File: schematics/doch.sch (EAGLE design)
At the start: 6 parts

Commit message: Продолжение работы над платами
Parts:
- added LP5907MFX-3.3: (no value), CanCubeSat:LP5907MFX-3.3
- added U$1: SD, CanCubeSat:SD

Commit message: 3я часть Дочернего балета
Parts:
- removed STM32F103C8T: STM32F103C8T, CanCubeSat:STM32F103C8T
- removed TOMOM: (no value), pinhead:PINHD-1X2
- added BUZZER: BUZZER, CanCubeSat:BUZZER
- added C1: 1nF, rcl:C-EUC0603
- added C15, C5, C6, C7, C8: 100nF, rcl:C-EUC0603
- added C16: 10µ, rcl:C-USC1206
- added C2: 10nF, rcl:C-EUC0603
- added IC2: STM32F103C8T, CanCubeSat:STM32F103C8T
- added JP1: (no value), pinhead:PINHD-1X5
- added PB5, PWR: (no value), led:LEDCHIPLED_0603
- added R1: 100R, rcl:R-US_R0603
- added R2: 10k, rcl:R-US_R0603
- added R27, R64, R79: 10k, resistor:R-US_R0603
- added R3: (no value), rcl:R-US_R0603
- added R81, R82: 2k, resistor:R-US_R0603
- added SD-PORT: SD, CanCubeSat:SD
- added TCXO: OC2E08000XCCDRX, CanCubeSat:OC2E08000XCCDRX
- added TOMA: (no value), pinhead:PINHD-1X2/90
- U$1: value SD -> SI2302CDS; device CanCubeSat:SD -> CanCubeSat:SI2302CDS
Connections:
- new net 3V3: C15.1, C16.1, C2.2, C5.1, C6.1, C7.1, C8.1, IC2.VBAT, IC2.VDD, IC2.VDDA, PB5.A, PWR.A, R27.1, R64.1, R79.1, TCXO.EN/DIS, TCXO.VCC
- new net 3V7: SUPPLY.1
- new net GND: C15.2, C16.2, C2.1, C5.2, C6.2, C7.2, C8.2, IC2.BOOT0, IC2.PB2, IC2.VSSA, R3.2, R82.1, SUPPLY.2, TCXO.GND, TOMA.2
- new net N$1: BUZZER.-, U$1.D
- new net N$10: R3.1
- new net N$159: PWR.C, R82.2
- new net N$161: IC2.PB5, R81.1
- new net N$17: PB5.C, R81.2
- new net N$2: R1.2, U$1.G
- new net N$3: R1.1, R2.2, U$1.S
- new net N$4: C1.2, TCXO.OUTPUT
- new net N$5: C1.1, IC2.OSC_IN
- new net N$6: R2.1
- new net N$7: BUZZER.+
- new net NRST: IC2.NRST, R79.2
- new net PE12: TOMA.1
- new net SWC: IC2.PA14, R27.2
- new net SWD: IC2.PA13, R64.2
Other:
- note added: "Микроконтроллер"
- moved on the sheet: BME280, GOOUUUATGM336H, LP5907MFX-3.3, LSM6DS3, SUPPLY

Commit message: Актуальная версия плат (и библиотеки)
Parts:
- removed SD-PORT: SD, CanCubeSat:SD
- added C10, C9: 1μF, rcl:C-EUC0603
- added C11, C12, C3, C4: 100nF, rcl:C-EUC0603
- added R4: 10K, rcl:R-US_R0603
- added R5: 100R, rcl:R-US_R0603
- added SD: SD-SPI, CanCubeSat:SD-SPI
- R3: value (none) -> 10K
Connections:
- removed net N$10: R3.1
- removed net N$3: R1.1, R2.2, U$1.S
- removed net N$6: R2.1
- removed net N$7: BUZZER.+
- removed net PE12: TOMA.1
- new net N$12: IC2.PC15
- new net N$8: R3.1, R5.1, TOMA.1
- new net N$9: IC2.PB0, R3.2
- new net PB1-BUZZER: IC2.PB1, R1.1, R2.2, U$1.S
- new net SPI1_CS_BME280: BME280.CSB, IC2.PC13
- new net SPI1_CS_LSM6DS3: IC2.PC14, LSM6DS3.CS
- new net SPI1_MISO: BME280.SDO, IC2.PA6, LSM6DS3.SA0
- new net SPI1_MOSI: BME280.SDI, IC2.PA7, LSM6DS3.SDA
- new net SPI1_SCK: BME280.SCK, IC2.PA5, LSM6DS3.SCL
- new net SPI2_CS_SD: IC2.PB12, SD.CS
- new net SPI2_MISO: IC2.PB14, R4.1, SD.DO
- new net SPI2_MOSI: IC2.PB15, SD.DI
- new net SPI2_SCK: IC2.PB13, SD.SCLK
- new net USART3_RX: GOOUUUATGM336H.TX, IC2.PB11
- new net USART3_TX: GOOUUUATGM336H.RX, IC2.PB10
- new net WKUP: IC2.PA0-WKUP, JP1.1
- net 3V3: now also BME280.VDD, BME280.VIO, BUZZER.+, C10.2, C11.2, C12.1, C3.2, C4.1, GOOUUUATGM336H.VCC, JP1.4, LP5907MFX-3.3.OUT, LSM6DS3.INT2, LSM6DS3.VDD, R5.2, SD.VDD
- net 3V7: now also C9.2, LP5907MFX-3.3.EN, LP5907MFX-3.3.IN
- net GND: now also BME280.GND, C10.1, C11.1, C12.2, C3.1, C4.2, C9.1, GOOUUUATGM336H.GND, LP5907MFX-3.3.GND, LSM6DS3.GND, LSM6DS3.SCX, LSM6DS3.SDX, R2.1, R4.2, SD.VSS; no longer R3.2
- net NRST: now also JP1.5
- net SWC: now also JP1.2
- net SWD: now also JP1.3
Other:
- moved on the sheet: BUZZER, C1, C15, C16, C2, C5, C6, C7, C8, IC2, JP1, LP5907MFX-3.3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

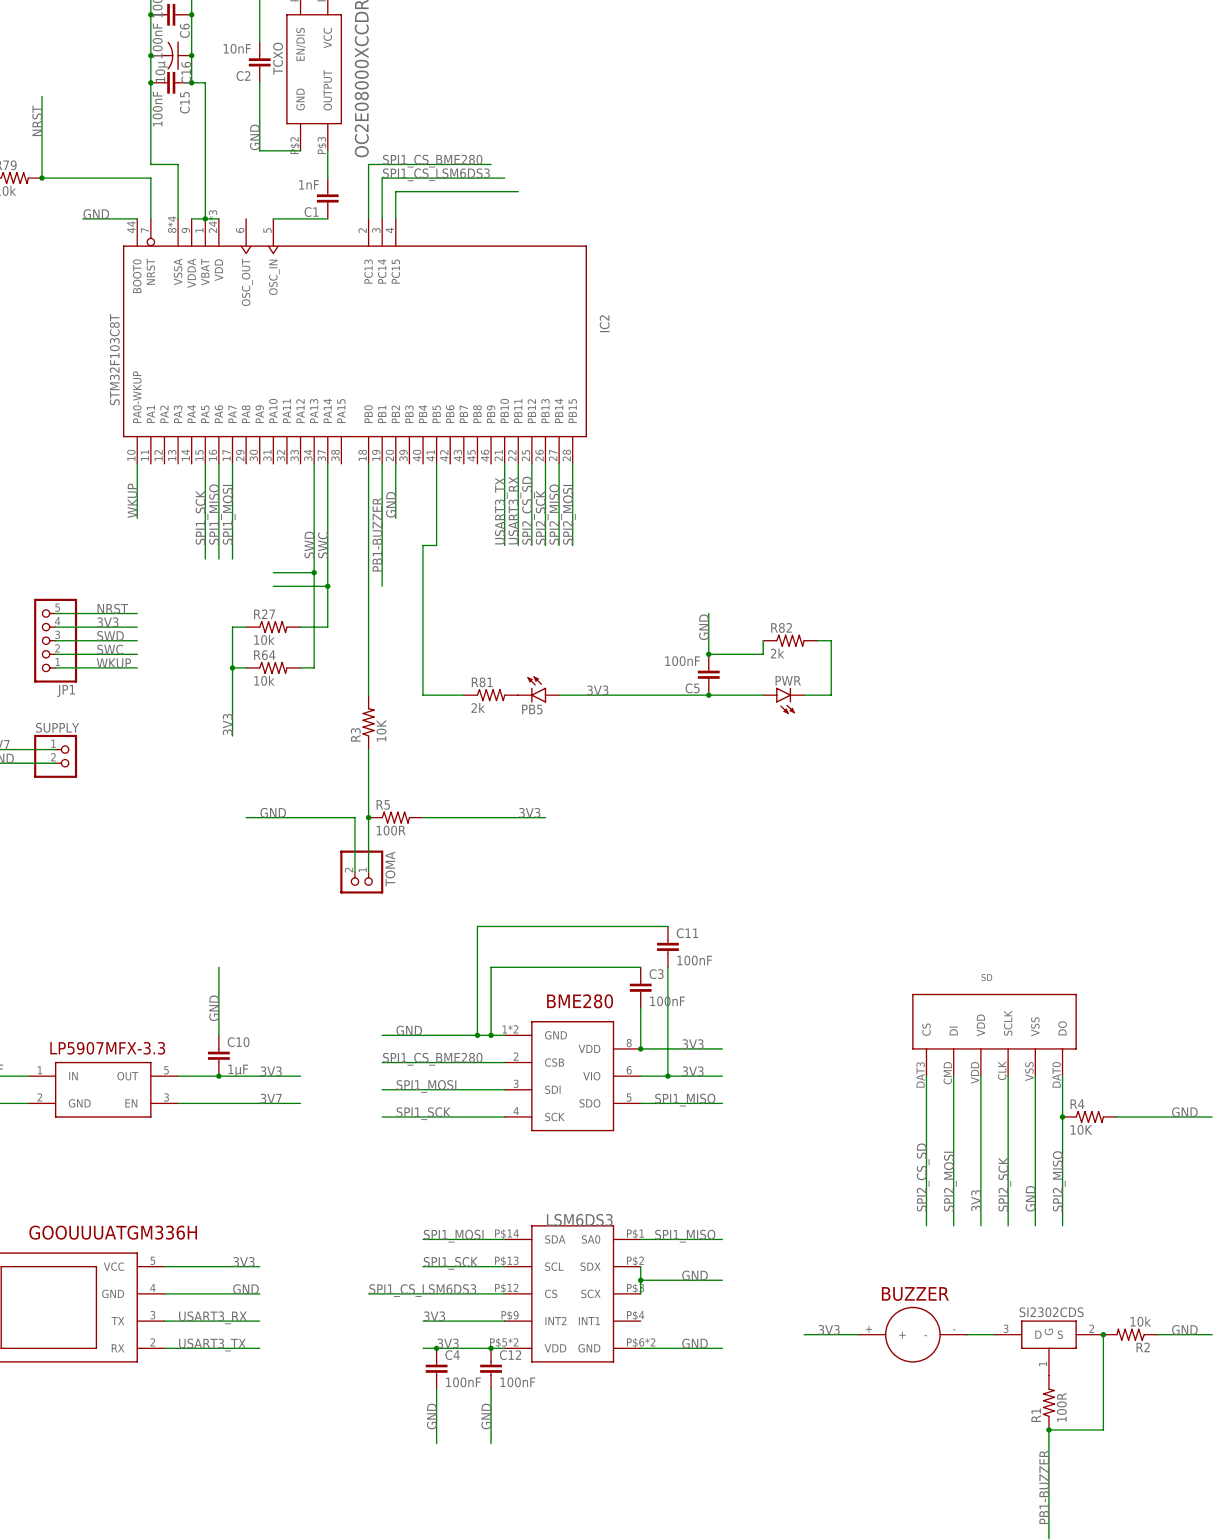
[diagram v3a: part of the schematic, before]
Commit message: Начал работу над физической платой, добавил радио
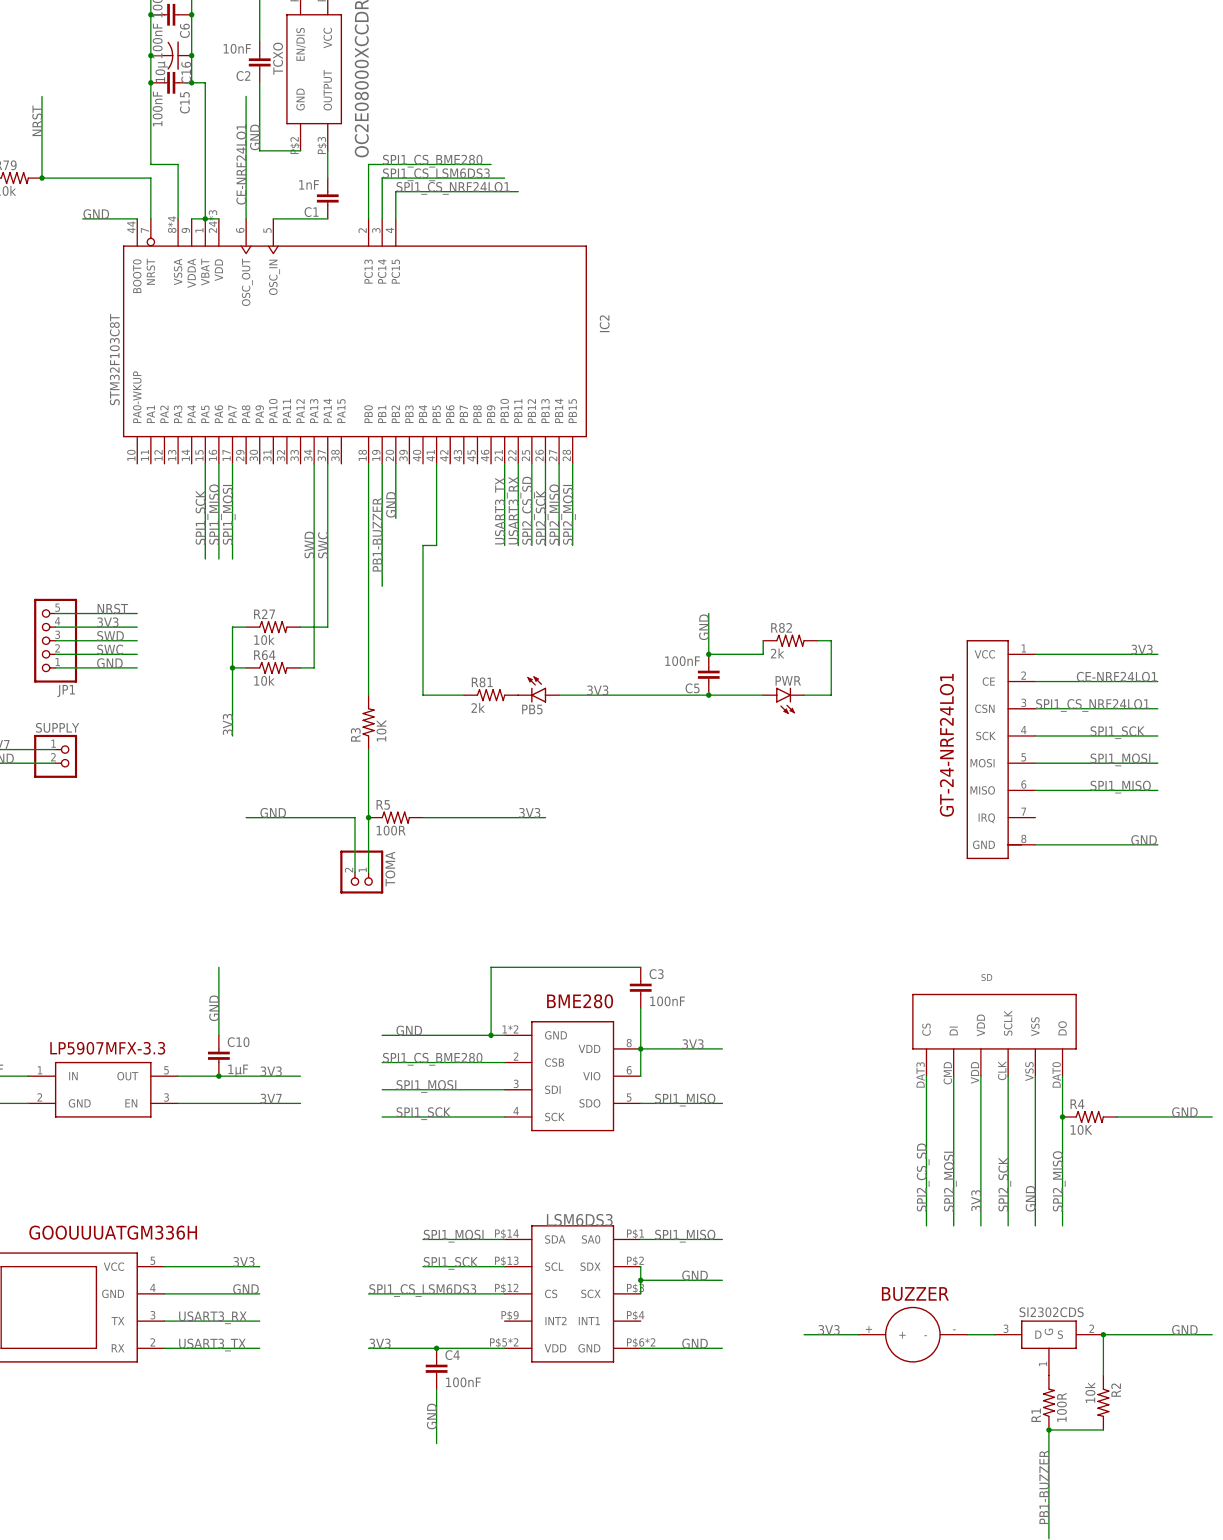
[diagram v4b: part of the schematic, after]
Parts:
- removed C11, C12: 100nF, rcl:C-EUC0603
- added GT-24-NRF24LO1: GT-24-NRF24LO1, CanCubeSat:GT-24-NRF24LO1
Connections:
- removed net N$12: IC2.PC15
- removed net WKUP: IC2.PA0-WKUP, JP1.1
- new net CE-NRF24LO1: GT-24-NRF24LO1.CE, IC2.OSC_OUT
- new net SPI1_CS_NRF24LO1: GT-24-NRF24LO1.CSN, IC2.PC15
- net 3V3: now also GT-24-NRF24LO1.VCC; no longer C11.2, C12.1, LSM6DS3.INT2
- net GND: now also GT-24-NRF24LO1.GND, JP1.1, U$1.S; no longer C11.1, C12.2
- net PB1-BUZZER: no longer U$1.S
- net SPI1_MISO: now also GT-24-NRF24LO1.MISO
- net SPI1_MOSI: now also GT-24-NRF24LO1.MOSI
- net SPI1_SCK: now also GT-24-NRF24LO1.SCK
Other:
- moved on the sheet: R2
